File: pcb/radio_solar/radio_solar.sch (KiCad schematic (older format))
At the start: 23 parts, among them J1 Conn_01x03, J2 Conn_01x02, J3 Conn_01x02, Q1 BC548, Q2 BC548, Q3 BC548, SW1 SW_DPST_x2

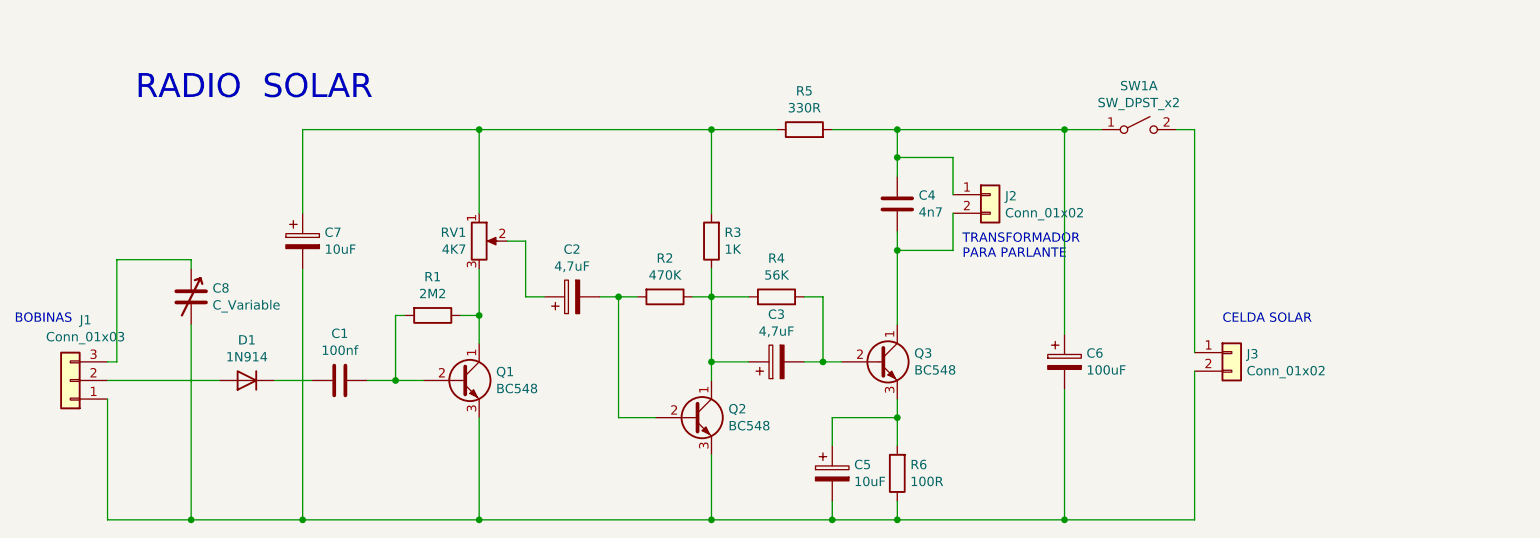
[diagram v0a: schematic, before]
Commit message: Se agrega la baterìa como fuente de alimentación
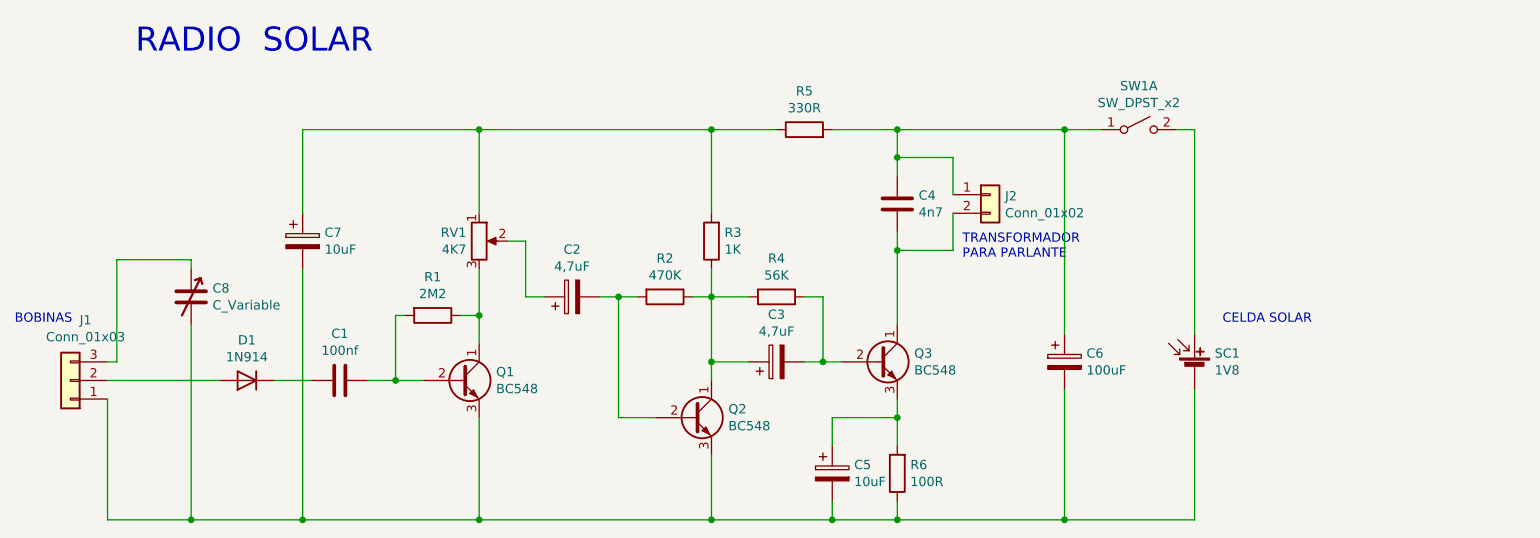
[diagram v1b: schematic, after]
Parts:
- removed J3: Conn_01x02, symbol Connector_Generic:Conn_01x02
- added SC1: 1V8, symbol Device:Solar_Cell
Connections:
- net at C5.2, C6.2, C7.2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: now also SC1.2 (-)
- net at SW1.2 (B): now also SC1.1 (+)
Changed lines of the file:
@@
 Wire Wire Line
 	7200 3400 7200 3800
-$Comp
-L Connector_Generic:Conn_01x02 J3
-U 1 1 5F782A2B
-P 9000 3950
-F 0 "J3" H 9080 3942 50  0000 L CNN
-F 1 "Conn_01x02" H 9080 3851 50  0000 L CNN
-F 2 "" H 9000 3950 50  0001 C CNN
-F 3 "~" H 9000 3950 50  0001 C CNN
-	1    9000 3950
-	1    0    0    -1
-$EndComp
 Wire Wire Line
 	8700 2750 8800 2750
-Wire Wire Line
-	8800 2750 8800 3950
-Wire Wire Line
-	8800 4050 8800 4850
 Wire Wire Line
 	8800 4850 8100 4850
@@
 	1    0    0    -1
 $EndComp
-Text Notes 3100 2600 0    129  ~ 0
+Text Notes 3100 2350 0    129  ~ 0
 RADIO  SOLAR
 Text Notes 2450 3800 0    50   ~ 0
@@
 Text Notes 7550 3450 0    50   ~ 0
 TRANSFORMADOR \nPARA PARLANTE
+$Comp
+L Device:Solar_Cell SC1
+U 1 1 5F954CD2
+P 8800 4050
+F 0 "SC1" H 8908 4146 50  0000 L CNN
+F 1 "1V8" H 8908 4055 50  0000 L CNN
+F 2 "" V 8800 4110 50  0001 C CNN
+F 3 "~" V 8800 4110 50  0001 C CNN
+	1    8800 4050
+	1    0    0    -1
+$EndComp
+Wire Wire Line
+	8800 3850 8800 2750
+Wire Wire Line
+	8800 4850 8800 4150
 $EndSCHEMATC

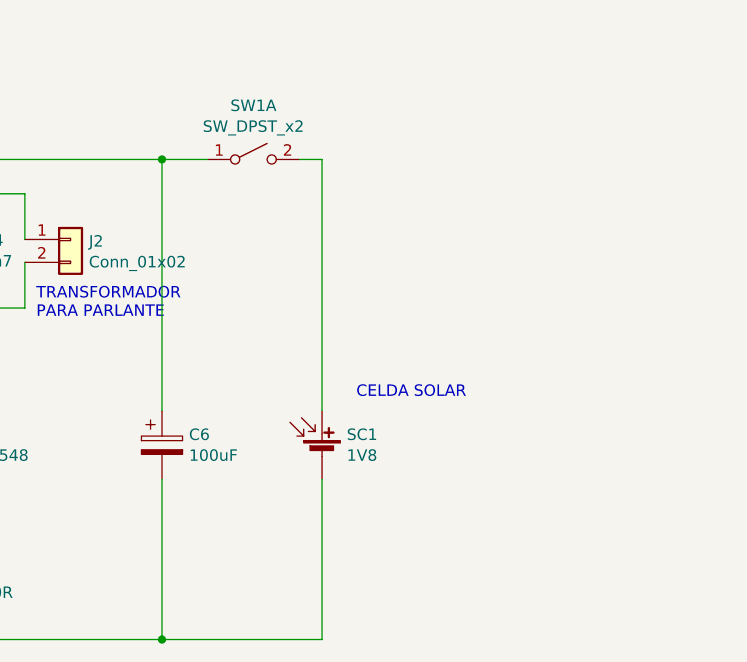
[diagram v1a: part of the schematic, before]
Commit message: se agrega label para vcc y gnd de la batería
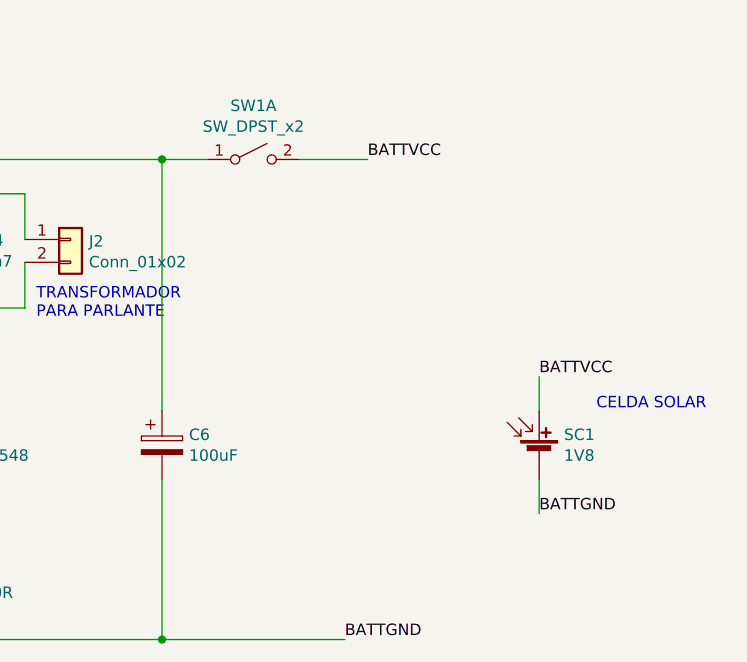
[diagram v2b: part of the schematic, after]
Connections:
- net BATTGND: now reaches C5.2, C6.2, C7.2, C8.2, J1.1 (Pin_1), Q1.3 (E), Q2.3 (E), R6.1, SC1.2 (-)
- net BATTVCC: now reaches SC1.1 (+), SW1.2 (B)
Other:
- moved on the sheet: SC1
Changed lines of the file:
@@
 Wire Wire Line
 	7200 3400 7200 3800
-Wire Wire Line
-	8700 2750 8800 2750
-Wire Wire Line
-	8800 4850 8100 4850
 Connection ~ 8100 4850
 Wire Wire Line
@@
 Text Notes 2450 3800 0    50   ~ 0
 BOBINAS
-Text Notes 8950 3800 0    50   ~ 0
+Text Notes 10000 3850 0    50   ~ 0
 CELDA SOLAR
 Text Notes 7550 3450 0    50   ~ 0
@@
 L Device:Solar_Cell SC1
 U 1 1 5F954CD2
-P 8800 4050
-F 0 "SC1" H 8908 4146 50  0000 L CNN
-F 1 "1V8" H 8908 4055 50  0000 L CNN
-F 2 "" V 8800 4110 50  0001 C CNN
-F 3 "~" V 8800 4110 50  0001 C CNN
-	1    8800 4050
+P 9750 4050
+F 0 "SC1" H 9858 4146 50  0000 L CNN
+F 1 "1V8" H 9858 4055 50  0000 L CNN
+F 2 "" V 9750 4110 50  0001 C CNN
+F 3 "~" V 9750 4110 50  0001 C CNN
+	1    9750 4050
 	1    0    0    -1
 $EndComp
 Wire Wire Line
-	8800 3850 8800 2750
+	8100 4850 8900 4850
+Text Label 9750 3700 0    50   ~ 0
+BATTVCC
 Wire Wire Line
-	8800 4850 8800 4150
+	9750 3850 9750 3700
+Text Label 9000 2750 0    50   ~ 0
+BATTVCC
+Wire Wire Line
+	8700 2750 9000 2750
+Text Label 9750 4300 0    50   ~ 0
+BATTGND
+Wire Wire Line
+	9750 4150 9750 4300
+Text Label 8900 4850 0    50   ~ 0
+BATTGND
 $EndSCHEMATC
